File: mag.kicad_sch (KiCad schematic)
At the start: 4 parts, among them U3 LIS3MDL

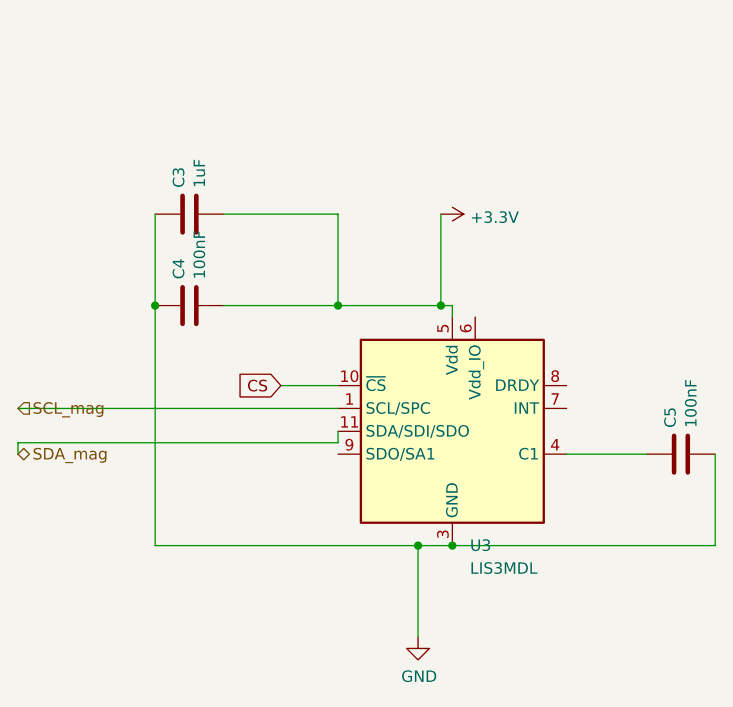
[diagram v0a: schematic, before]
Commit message: Magnetometer fixes\n\nCloses #2
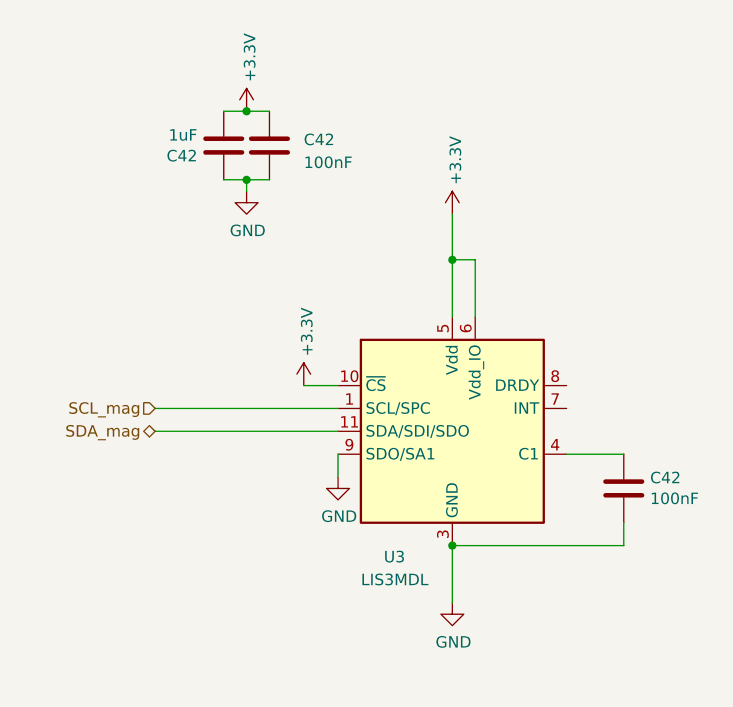
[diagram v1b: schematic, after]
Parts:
- renumbered C5 to C42, C3 to C42, C4 to C42
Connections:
- net CS is gone; now on net +3V3: U3.10 (~{CS})
- net +3V3: now also U3.6 (Vdd_IO)
- net GND: now also U3.9 (SDO/SA1)
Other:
- moved on the sheet: C42

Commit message: Clean-up schematic
Closes #4
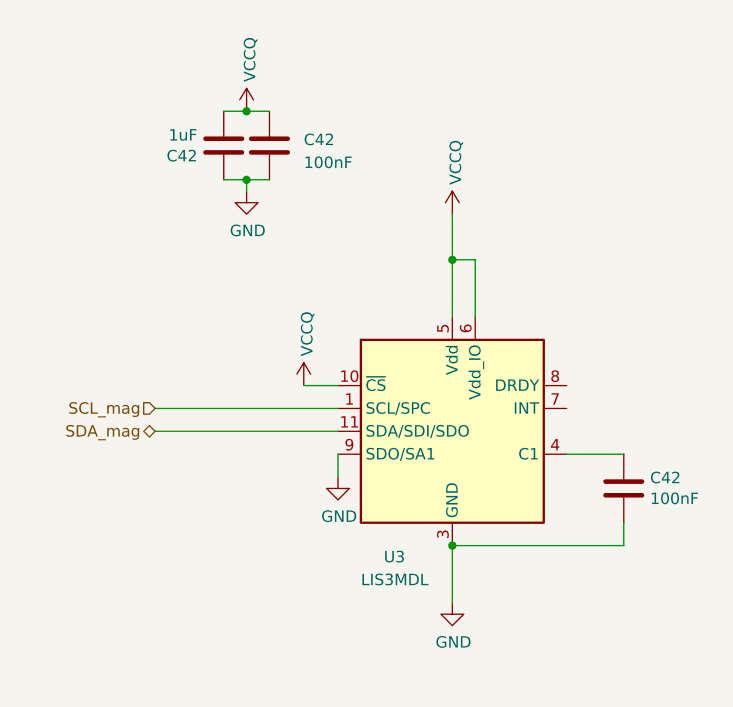
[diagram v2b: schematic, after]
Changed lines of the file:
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@@
       (effects (font (size 1.27 1.27)) hide)
     )
-    (property "Value" "+3.3V" (at 136.271 79.2988 90)
+    (property "Value" "VCCQ" (at 136.271 79.2988 90)
       (effects (font (size 1.27 1.27)) (justify left))
     )
@@
       (effects (font (size 1.27 1.27)) hide)
     )
-    (property "Value" "+3.3V" (at 119.761 98.3488 90)
+    (property "Value" "VCCQ" (at 119.761 98.3488 90)
       (effects (font (size 1.27 1.27)) (justify left))
     )
@@
       (effects (font (size 1.27 1.27)) hide)
     )
-    (property "Value" "+3.3V" (at 113.411 67.8688 90)
-      (effects (font (size 1.27 1.27)) (justify left))
-    )
+    (property "Value" "VCCQ" (at 113.411 67.8688 90)
+      (effects (font (size 1.27 1.27)) (justify left))
+    )

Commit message: Add I2C multiplexer
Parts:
- removed C42 (x2): 100nF, Capacitor_SMD:C_0603_1608Metric, symbol Device:C
- removed C42: 1uF, Capacitor_SMD:C_0603_1608Metric, symbol Device:C
- removed U3: LIS3MDL, Package_LGA:LGA-12_2x2mm_P0.5mm, symbol Sensor_Magnetic:LIS3MDL
